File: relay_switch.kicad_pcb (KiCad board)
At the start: 2 copper layers, 37.1 x 73.4 mm, 19 parts, among them P1 POWER, P2 CONN_01X04, P3 INPUT_1, P4 INPUT_2, P5 INPUT_3, P6 INPUT_4, P7 OUTPUT, U1 ULN2003A

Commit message: rerouted pcb
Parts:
- removed REF** (x4): 3.5mmM3, mechanical:3.5mm_m3
- added P10: j_INPUT_2, w_conn_jst-ph:b3b-ph-kl, F.Cu at (208.0, 58.0)
- added P11: j_INPUT_3, w_conn_jst-ph:b3b-ph-kl, F.Cu at (208.0, 76.0)
- added P12: j_INPUT_4, w_conn_jst-ph:b3b-ph-kl, F.Cu at (208.0, 94.0)
- added P13: JST_POWER, w_conn_jst-ph:b2b-ph-kl, F.Cu at (214.5, 22.5)
- added P14: CONN_01X04_jst, w_conn_jst-ph:b4b-ph-kl, F.Cu at (236.0, 40.0)
- added P15: MOUNTING_HOLE, mechanical:3.5mm_m3, F.Cu at (239.5, 20.0)
- added P16: MOUNTING_HOLE, mechanical:3.5mm_m3, F.Cu at (239.5, 106.6)
- added P17: MOUNTING_HOLE, mechanical:3.5mm_m3, F.Cu at (204.0, 20.1)
- added P18: MOUNTING_HOLE, mechanical:3.5mm_m3, F.Cu at (204.0, 106.6)
- added P8: j_OUTPUT, w_conn_screw:mstbva_2,5%2f3-g-5,08, F.Cu at (238.0, 67.0)
- added P9: j_INPUT_1, w_conn_jst-ph:b3b-ph-kl, F.Cu at (208.0, 40.0)
- P3, P4, P5, P6, P7: footprint Pin_Headers:Pin_Header_Straight_1x03 -> w_conn_screw:mstbva_2,5%2f3-g-5,08
- RLY1, RLY2, RLY3, RLY4: footprint Relays_ThroughHole:RY12w-k -> Relays_ThroughHole:RY12w-k_bigger_holes
- moved P7 129.1 mm to (271.0, 71.0), turned to 270 degrees
- moved RLY1 116.0 mm to (231.5, 45.0), turned to 180 degrees
- moved RLY2 114.3 mm to (231.7, 63.1), turned to 180 degrees
- moved RLY3 113.0 mm to (231.7, 80.6), turned to 180 degrees
- moved RLY4 111.3 mm to (231.5, 99.0), turned to 180 degrees
- moved D1 104.3 mm to (225.5, 21.0), turned to 180 degrees
- moved U1 103.5 mm to (221.9, 29.2)
- moved R1 101.8 mm to (235.0, 28.5), turned to 90 degrees
- moved P2 101.7 mm to (233.5, 36.5), turned to 0 degrees
- moved P3 99.3 mm to (205.0, 40.0), turned to 90 degrees
- moved P4 96.8 mm to (205.0, 58.0), turned to 90 degrees
- moved P5 94.5 mm to (205.0, 76.0), turned to 90 degrees
- moved P7 94.1 mm to (234.5, 64.5)
- moved P6 92.5 mm to (205.0, 94.0), turned to 90 degrees
- moved P1 87.2 mm to (215.5, 20.5), turned to 270 degrees
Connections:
- RLY1 pad 8: GND -> +12V
- RLY2 pad 8: GND -> +12V
- RLY3 pad 8: GND -> +12V
- RLY4 pad 8: GND -> +12V
- U1 pad 9: +12V -> GND
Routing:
- net GND: track 128.1 -> 25.3 mm
- net +12V: track 15.5 -> 92.8 mm, vias 1 -> 0
- net R_OUT: track 54.4 -> 88.9 mm, vias 2 -> 0
- net L_OUT: track 57.8 -> 84.9 mm, vias 0 -> 1
- net Net-(P14-Pad4): track 6.83 -> 26.5 mm
- net Net-(P14-Pad3): track 6.83 -> 23.1 mm
- net Net-(P14-Pad2): track 6.83 -> 18.8 mm
- net Net-(RLY4-Pad1): track 56.9 -> 67.9 mm
- net R2_GND: track 97.0 -> 106.4 mm, vias 3 -> 0
- net Net-(P14-Pad1): track 7.40 -> 15.5 mm
- net Net-(RLY3-Pad1): track 42.2 -> 48.6 mm
- net R4_L_IN: track 20.1 -> 14.6 mm
- net R1_L_IN: track 19.0 -> 14.6 mm
- net Net-(D1-Pad1): track 15.5 -> 11.1 mm, vias 1 -> 0
- net Net-(RLY1-Pad1): track 18.5 -> 14.2 mm
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- removed copper zone on B.Cu, net R2_GND
- removed copper zone on F.Cu, net R2_GND
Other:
- board size 37.1 x 73.4 mm -> 229.9 x 105.2 mm

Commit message: couple misc changes, trying to finalize the pcb
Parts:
- moved P7 35.6 mm to (238.4, 85.4)
- moved P14 3.38 mm to (239.3, 40.5)
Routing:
- net Net-(P14-Pad1): track 15.5 -> 20.3 mm
- net Net-(P14-Pad3): track 23.1 -> 27.0 mm
- net Net-(P14-Pad2): track 18.8 -> 22.4 mm
- net Net-(P14-Pad4): track 26.5 -> 29.6 mm
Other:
- board size 229.9 x 105.2 mm -> 41.5 x 92.5 mm
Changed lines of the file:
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@@
-(kicad_pcb (version 4) (host pcbnew 0.201506172246+5766~23~ubuntu14.04.1-product)
+(kicad_pcb (version 4) (host pcbnew 0.201508290901+6132~28~ubuntu14.04.1-product)
   (general
     (links 61)
-    (no_connects 61)
-    (area 115.519999 67.767999 152.704001 141.274001)
+    (no_connects 4)
+    (area 200.949999 16.949999 242.550001 109.550001)
     (thickness 1.6)
-    (drawings 173)
-    (tracks 187)
+    (drawings 171)
+    (tracks 191)
     (zones 0)
     (modules 26)
@@
   )
   (setup
-    (last_trace_width 0.75)
+    (last_trace_width 0.25)
     (user_trace_width 0.75)
     (trace_clearance 0.2)
@@
   )
   (module w_conn_screw:mstbva_2,5%2f3-g-5,08 (layer F.Cu)
-    (at 271 71 270)
+    (at 238.4044 85.3694 270)
     (descr "Terminal block 3 pins, Phoenix MSTBVA 2,5/3-G-5,08")
     (tags DEV)
@@
   )
   (module w_conn_jst-ph:b4b-ph-kl (layer F.Cu)
-    (at 236 40.00228 270)
+    (at 239.3442 40.48506 270)
     (descr "JST PH series connector, B4B-PH-KL")
     (fp_text reference P14 (at 0 -2.99974 270) (layer F.SilkS)
@@
     )
   )
+  (dimension 92.5068 (width 0.3) (layer Eco2.User)
+    (gr_text "92.507 mm" (at 252.556 63.246 270) (layer Eco2.User)
+      (effects (font (size 1.5 1.5) (thickness 0.3)))
+    )
+    (feature1 (pts (xy 242.4938 109.4994) (xy 253.906 109.4994)))
+    (feature2 (pts (xy 242.4938 16.9926) (xy 253.906 16.9926)))
+    (crossbar (pts (xy 251.206 16.9926) (xy 251.206 109.4994)))
+    (arrow1a (pts (xy 251.206 109.4994) (xy 250.619579 108.372896)))
+    (arrow1b (pts (xy 251.206 109.4994) (xy 251.792421 108.372896)))
+    (arrow2a (pts (xy 251.206 16.9926) (xy 250.619579 18.119104)))
+    (arrow2b (pts (xy 251.206 16.9926) (xy 251.792421 18.119104)))
+  )
+  (dimension 41.4782 (width 0.3) (layer Eco2.User)
+    (gr_text "41.478 mm" (at 221.7547 116.666) (layer Eco2.User)
+      (effects (font (size 1.5 1.5) (thickness 0.3)))
+    )
+    (feature1 (pts (xy 242.4938 109.4994) (xy 242.4938 118.016)))
+    (feature2 (pts (xy 201.0156 109.4994) (xy 201.0156 118.016)))
+    (crossbar (pts (xy 201.0156 115.316) (xy 242.4938 115.316)))
+    (arrow1a (pts (xy 242.4938 115.316) (xy 241.367296 115.902421)))
+    (arrow1b (pts (xy 242.4938 115.316) (xy 241.367296 114.729579)))
+    (arrow2a (pts (xy 201.0156 115.316) (xy 202.142104 115.902421)))
+    (arrow2b (pts (xy 201.0156 115.316) (xy 202.142104 114.729579)))
+  )
   (gr_line (start 201 17) (end 242.5 17) (layer Edge.Cuts) (width 0.1))
   (gr_line (start 201 109.5) (end 201 17) (layer Edge.Cuts) (width 0.1))
@@
   (gr_line (start 148.844 80.518) (end 152.4 80.518) (angle 90) (layer B.SilkS) (width 0.2))
   (gr_line (start 148.844 74.422) (end 148.844 80.518) (angle 90) (layer B.SilkS) (width 0.2))
-  (gr_line (start 49.654 122.224) (end 49.654 48.818) (angle 90) (layer Edge.Cuts) (width 0.1))
-  (gr_line (start 12.57 122.224) (end 49.654 122.224) (angle 90) (layer Edge.Cuts) (width 0.1))
-  (gr_line (start 12.57 48.818) (end 12.57 122.224) (angle 90) (layer Edge.Cuts) (width 0.1))
-  (gr_line (start 49.654 48.818) (end 12.57 48.818) (angle 90) (layer Edge.Cuts) (width 0.1))
   (gr_text G (at 148.336 75.438 90) (layer B.SilkS)
     (effects (font (size 0.8 0.8) (thickness 0.1)) (justify mirror))
@@
   (segment (start 208 57.99848) (end 205.00152 57.99848) (width 0.75) (layer F.Cu) (net 18))
   (segment (start 205.00152 57.99848) (end 205 58) (width 0.75) (layer F.Cu) (net 18))
+  (segment (start 233.5 36.46) (end 239.17086 36.46) (width 0.25) (layer F.Cu) (net 19))
+  (segment (start 239.17086 36.46) (end 239.3442 36.63334) (width 0.25) (layer F.Cu) (net 19))
+  (segment (start 239.3442 36.63334) (end 239.3442 37.48278) (width 0.25) (layer F.Cu) (net 19))
   (segment (start 233.5 36.46) (end 233.5 27.1515) (width 0.25) (layer F.Cu) (net 19))
   (segment (start 233.5 27.1515) (end 231.7285 25.38) (width 0.25) (layer F.Cu) (net 19))
   (segment (start 231.7285 25.38) (end 230.78 25.38) (width 0.25) (layer F.Cu) (net 19))
-  (segment (start 236 37) (end 234.04 37) (width 0.25) (layer F.Cu) (net 19))
   (segment (start 234.04 37) (end 233.5 36.46) (width 0.25) (layer F.Cu) (net 19))
+  (segment (start 233.5 39) (end 238.8599 39) (width 0.25) (layer F.Cu) (net 20))
+  (segment (start 238.8599 39) (end 239.3442 39.4843) (width 0.25) (layer F.Cu) (net 20))
   (segment (start 228.24 25.38) (end 228.38 25.38) (width 0.25) (layer F.Cu) (net 20))
   (segment (start 228.38 25.38) (end 231.5 28.5) (width 0.25) (layer F.Cu) (net 20))
@@
   (segment (start 232.5 37.648601) (end 232.5 38.1524) (width 0.25) (layer F.Cu) (net 20))
   (segment (start 233.3476 39) (end 233.5 39) (width 0.25) (layer F.Cu) (net 20))
-  (segment (start 236 39.00152) (end 233.50152 39.00152) (width 0.25) (layer F.Cu) (net 20))
   (segment (start 233.50152 39.00152) (end 233.5 39) (width 0.25) (layer F.Cu) (net 20))
+  (segment (start 233.5 41.54) (end 239.29002 41.54) (width 0.25) (layer F.Cu) (net 21))
+  (segment (start 239.29002 41.54) (end 239.3442 41.48582) (width 0.25) (layer F.Cu) (net 21))
   (segment (start 225.7 25.38) (end 226.38 25.38) (width 0.25) (layer F.Cu) (net 21))
   (segment (start 226.38 25.38) (end 230 29) (width 0.25) (layer F.Cu) (net 21))
@@
   (segment (start 231.5 39.6924) (end 233.3476 41.54) (width 0.25) (layer F.Cu) (net 21))
   (segment (start 233.3476 41.54) (end 233.5 41.54) (width 0.25) (layer F.Cu) (net 21))
-  (segment (start 236 41.00304) (end 234.03696 41.00304) (width 0.25) (layer F.Cu) (net 21))
   (segment (start 234.03696 41.00304) (end 233.5 41.54) (width 0.25) (layer F.Cu) (net 21))
+  (segment (start 233.5 44.08) (end 238.749 44.08) (width 0.25) (layer F.Cu) (net 22))
+  (segment (start 238.749 44.08) (end 239.3442 43.4848) (width 0.25) (layer F.Cu) (net 22))
   (segment (start 223.16 25.38) (end 223.88 25.38) (width 0.25) (layer F.Cu) (net 22))
   (segment (start 229.204999 32.450217) (end 229.263501 32.508719) (width 0.25) (layer F.Cu) (net 22))
@@
   (segment (start 230.5 41.2324) (end 233.3476 44.08) (width 0.25) (layer F.Cu) (net 22))
   (segment (start 233.3476 44.08) (end 233.5 44.08) (width 0.25) (layer F.Cu) (net 22))
-  (segment (start 236 43.00202) (end 234.57798 43.00202) (width 0.25) (layer F.Cu) (net 22))
-  (segment (start 234.57798 43.00202) (end 233.5 44.08) (width 0.25) (layer F.Cu) (net 22))
 )

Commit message: board almost finished
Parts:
- removed P15, P16, P17, P18: MOUNTING_HOLE, mechanical:3.5mm_m3
- removed P5: INPUT_3, w_conn_screw:mstbva_2,5%2f3-g-5,08
- removed P6: INPUT_4, w_conn_screw:mstbva_2,5%2f3-g-5,08
- removed P7: OUTPUT, Pin_Headers:Pin_Header_Straight_1x03
- removed P7: OUTPUT, w_conn_screw:mstbva_2,5%2f3-g-5,08
- D1: footprint LEDs:LED-5MM -> LEDs:LED-1206
- P1: value POWER -> board_mount; footprint Pin_Headers:Pin_Header_Straight_1x02 -> mechanical:3.5mm_m3
- P10: value j_INPUT_2 -> INPUT2
- P11: value j_INPUT_3 -> INPUT3
- P12: value j_INPUT_4 -> INPUT4
- P13: value JST_POWER -> 12vdc
- P14: value CONN_01X04_jst -> J_CONN_01X04
- P2: value CONN_01X04 -> board_mount; footprint Pin_Headers:Pin_Header_Straight_1x04 -> mechanical:3.5mm_m3
- P3: value INPUT_1 -> board_mount; footprint w_conn_screw:mstbva_2,5%2f3-g-5,08 -> mechanical:3.5mm_m3
- P4: value INPUT_2 -> board_mount; footprint w_conn_screw:mstbva_2,5%2f3-g-5,08 -> mechanical:3.5mm_m3
- P8: value j_OUTPUT -> OUTPUT; footprint w_conn_screw:mstbva_2,5%2f3-g-5,08 -> w_conn_jst-ph:b3b-ph-kl
- P9: value j_INPUT_1 -> INPUT1
- R1: footprint Resistors_ThroughHole:Resistor_Horizontal_RM10mm -> Resistors_SMD:R_1206_HandSoldering; moved to B.Cu
- U1: footprint Sockets_DIP:DIP-16__300 -> Housings_SSOP:SSOP-16_4.4x5.2mm_Pitch0.65mm
- moved P2 163.1 mm to (134.5, 166.1)
- moved P1 157.9 mm to (154.2, 166.0), turned to 0 degrees
- moved P8 135.2 mm to (145.5, 165.6), turned to 0 degrees
- moved R1 123.2 mm to (147.7, 115.4), turned to 0 degrees
- moved U1 121.1 mm to (139.6, 118.0), turned to 0 degrees
- moved P14 119.9 mm to (142.9, 111.7), turned to 180 degrees
- moved D1 117.9 mm to (149.6, 111.2), turned to 270 degrees
- moved RLY1 114.0 mm to (156.9, 131.2)
- moved P9 114.0 mm to (133.6, 126.3)
- moved P13 113.0 mm to (153.9, 117.9), turned to 90 degrees
- moved RLY2 108.3 mm to (157.0, 141.5)
- moved P10 108.2 mm to (133.6, 136.6)
- moved RLY3 103.4 mm to (157.0, 152.1)
- moved P11 103.2 mm to (133.7, 147.5)
- moved P3 100.4 mm to (134.5, 111.5), turned to 0 degrees
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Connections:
- P1 pad 1: +12V -> (no net)
- P10 pad 2: R2_GND -> G_OUT
- P11 pad 2: R2_GND -> G_OUT
- P12 pad 2: R2_GND -> G_OUT
- P14 pad 1: Net-(P14-Pad1) -> T1
- P14 pad 2: Net-(P14-Pad2) -> T2
- P14 pad 3: Net-(P14-Pad3) -> T3
- P14 pad 4: Net-(P14-Pad4) -> T4
- P2 pad 1: Net-(P14-Pad1) -> (no net)
- P3 pad 1: R1_R_IN -> (no net)
- P4 pad 1: R2_R_IN -> (no net)
- P8 pad 2: R2_GND -> G_OUT
- P9 pad 2: R2_GND -> G_OUT
- RLY1 pad 2: Net-(RLY1-Pad2) -> (no net)
- RLY1 pad 7: Net-(RLY1-Pad7) -> (no net)
- RLY2 pad 2: Net-(RLY2-Pad2) -> (no net)
- RLY2 pad 7: Net-(RLY2-Pad7) -> (no net)
- RLY3 pad 2: Net-(RLY3-Pad2) -> (no net)
- RLY3 pad 7: Net-(RLY3-Pad7) -> (no net)
- RLY4 pad 2: Net-(RLY4-Pad2) -> (no net)
- RLY4 pad 7: Net-(RLY4-Pad7) -> (no net)
- U1 pad 1: Net-(P14-Pad1) -> T1
- U1 pad 10: Net-(U1-Pad10) -> (no net)
- U1 pad 11: Net-(U1-Pad11) -> (no net)
- U1 pad 12: Net-(U1-Pad12) -> (no net)
- U1 pad 2: Net-(P14-Pad2) -> T2
- U1 pad 3: Net-(P14-Pad3) -> T3
- U1 pad 4: Net-(P14-Pad4) -> T4
- U1 pad 5: Net-(U1-Pad5) -> (no net)
- U1 pad 6: Net-(U1-Pad6) -> (no net)
- U1 pad 7: Net-(U1-Pad7) -> (no net)
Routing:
- net R2_GND: track 106.4 -> 0.00 mm
- net G_OUT: track 0.00 -> 59.0 mm
- net R_OUT: track 88.9 -> 41.8 mm
- net +12V: track 92.8 -> 48.7 mm, vias 0 -> 1
- net L_OUT: track 84.9 -> 52.9 mm, vias 1 -> 0
- net Net-(P14-Pad4): track 29.6 -> 0.00 mm
- net Net-(P14-Pad3): track 27.0 -> 0.00 mm
- net Net-(P14-Pad2): track 22.4 -> 0.00 mm
- net Net-(P14-Pad1): track 20.3 -> 0.00 mm
- net Net-(RLY4-Pad1): track 67.9 -> 51.1 mm
- net T1: track 0.00 -> 11.0 mm, vias 0 -> 1
- net T2: track 0.00 -> 10.1 mm
- net T3: track 0.00 -> 10.0 mm, vias 0 -> 1
- net T4: track 0.00 -> 8.78 mm, vias 0 -> 1
- net Net-(RLY1-Pad1): track 14.2 -> 22.3 mm
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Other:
- board size 41.5 x 92.5 mm -> 25.6 x 60.4 mm
- board text added: "12vdc"
- board text added: "2016"
- board text added: "INPUT1"
- board text added: "INPUT3"
- board text added: "INPUT4"
- board text added: "L.IN"
- board text added: "L.OUT"
- board text added: "R.IN"
- board text added: "R.OUT"
- board text added: "jjrh"
- board text removed: "10"
- board text removed: "10k"
- board text removed: "11"
- board text removed: "12"
- board text removed: "13"
- board text removed: "14"
- board text removed: "15"
- board text removed: "5"
- board text removed: "6"
- board text removed: "7"
- board text removed: "GND"
- board text removed: "INPUT 1"
- board text removed: "INPUT 2"
- board text removed: "INPUT 3"
- board text removed: "INPUT 4"
- board text removed: "INPUT BOARD V1"
- board text removed: "L"
- board text removed: "R"
- board text removed: "ULN2003A"
- board text removed: "jjrh 2015"

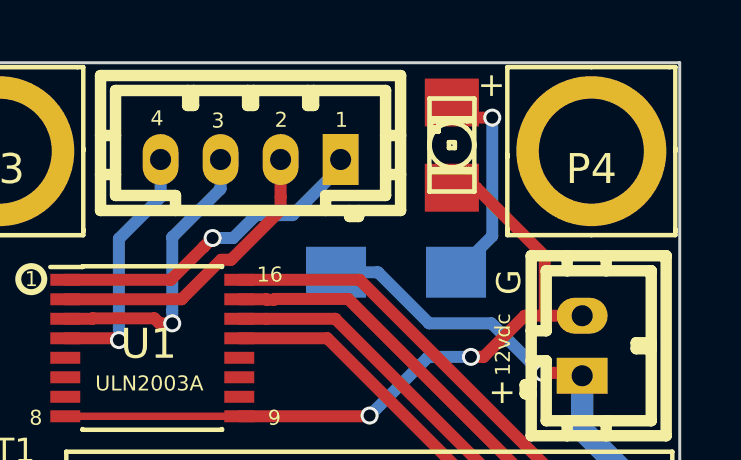
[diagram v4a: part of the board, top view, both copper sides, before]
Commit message: set 3d footprint for the led
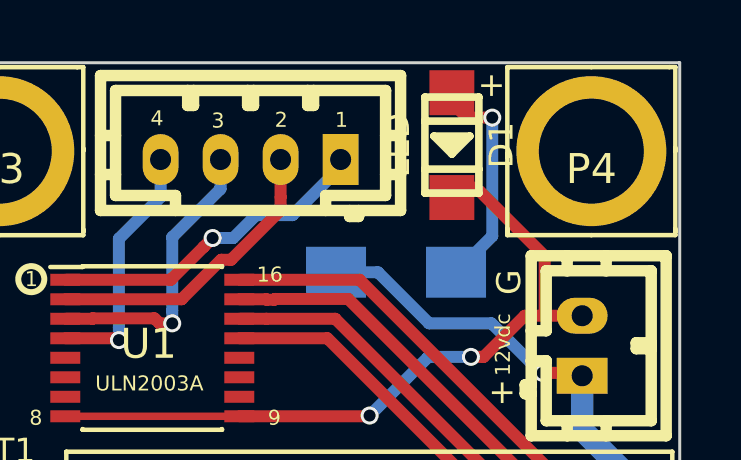
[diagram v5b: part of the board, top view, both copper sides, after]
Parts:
- D1: footprint LEDs:LED-1206 -> w_smd_leds:Led_1206
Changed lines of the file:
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@@
     )
-  )
-  (module LEDs:LED-1206 (layer F.Cu)
-    (at 149.5806 111.20374 270)
-    (descr "LED 1206 smd package")
-    (tags "LED1206 SMD")
-    (attr smd)
-    (fp_text reference D1 (at 0.254 -1.524 270) (layer F.SilkS) hide
-      (effects (font (size 1 1) (thickness 0.15)))
-    )
-    (fp_text value LED (at 0 1.65 270) (layer F.Fab) hide
-      (effects (font (size 1 1) (thickness 0.15)))
-    )
-    (fp_line (start 0.09906 0.09906) (end -0.09906 0.09906) (layer F.SilkS) (width 0.15))
-    (fp_line (start -0.09906 0.09906) (end -0.09906 -0.09906) (layer F.SilkS) (width 0.15))
-    (fp_line (start 0.09906 -0.09906) (end -0.09906 -0.09906) (layer F.SilkS) (width 0.15))
-    (fp_line (start 0.09906 0.09906) (end 0.09906 -0.09906) (layer F.SilkS) (width 0.15))
-    (fp_line (start -0.44958 0.6985) (end -0.79756 0.6985) (layer F.SilkS) (width 0.15))
-    (fp_line (start -0.79756 0.6985) (end -0.79756 0.44958) (layer F.SilkS) (width 0.15))
-    (fp_line (start -0.44958 0.44958) (end -0.79756 0.44958) (layer F.SilkS) (width 0.15))
-    (fp_line (start -0.44958 0.6985) (end -0.44958 0.44958) (layer F.SilkS) (width 0.15))
-    (fp_line (start -0.79756 0.6985) (end -0.89916 0.6985) (layer F.SilkS) (width 0.15))
-    (fp_line (start -0.89916 0.6985) (end -0.89916 -0.49784) (layer F.SilkS) (width 0.15))
-    (fp_line (start -0.79756 -0.49784) (end -0.89916 -0.49784) (layer F.SilkS) (width 0.15))
-    (fp_line (start -0.79756 0.6985) (end -0.79756 -0.49784) (layer F.SilkS) (width 0.15))
-    (fp_line (start -0.79756 -0.54864) (end -0.89916 -0.54864) (layer F.SilkS) (width 0.15))
-    (fp_line (start -0.89916 -0.54864) (end -0.89916 -0.6985) (layer F.SilkS) (width 0.15))
-    (fp_line (start -0.79756 -0.6985) (end -0.89916 -0.6985) (layer F.SilkS) (width 0.15))
-    (fp_line (start -0.79756 -0.54864) (end -0.79756 -0.6985) (layer F.SilkS) (width 0.15))
-    (fp_line (start 0.89916 0.6985) (end 0.79756 0.6985) (layer F.SilkS) (width 0.15))
-    (fp_line (start 0.79756 0.6985) (end 0.79756 -0.49784) (layer F.SilkS) (width 0.15))
-    (fp_line (start 0.89916 -0.49784) (end 0.79756 -0.49784) (layer F.SilkS) (width 0.15))
-    (fp_line (start 0.89916 0.6985) (end 0.89916 -0.49784) (layer F.SilkS) (width 0.15))
-    (fp_line (start 0.89916 -0.54864) (end 0.79756 -0.54864) (layer F.SilkS) (width 0.15))
-    (fp_line (start 0.79756 -0.54864) (end 0.79756 -0.6985) (layer F.SilkS) (width 0.15))
-    (fp_line (start 0.89916 -0.6985) (end 0.79756 -0.6985) (layer F.SilkS) (width 0.15))
-    (fp_line (start 0.89916 -0.54864) (end 0.89916 -0.6985) (layer F.SilkS) (width 0.15))
-    (fp_line (start -0.44958 0.6985) (end -0.59944 0.6985) (layer F.SilkS) (width 0.15))
-    (fp_line (start -0.59944 0.6985) (end -0.59944 0.44958) (layer F.SilkS) (width 0.15))
-    (fp_line (start -0.44958 0.44958) (end -0.59944 0.44958) (layer F.SilkS) (width 0.15))
-    (fp_line (start -0.44958 0.6985) (end -0.44958 0.44958) (layer F.SilkS) (width 0.15))
-    (fp_line (start -1.5494 0.7493) (end 1.5494 0.7493) (layer F.SilkS) (width 0.15))
-    (fp_line (start 1.5494 0.7493) (end 1.5494 -0.7493) (layer F.SilkS) (width 0.15))
-    (fp_line (start 1.5494 -0.7493) (end -1.5494 -0.7493) (layer F.SilkS) (width 0.15))
-    (fp_line (start -1.5494 -0.7493) (end -1.5494 0.7493) (layer F.SilkS) (width 0.15))
-    (fp_arc (start 0 0) (end -0.54864 0.49784) (angle -95.4) (layer F.SilkS) (width 0.15))
-    (fp_arc (start 0 0) (end 0.54864 0.49784) (angle -84.5) (layer F.SilkS) (width 0.15))
-    (fp_arc (start 0 0) (end 0.54864 -0.49784) (angle -95.4) (layer F.SilkS) (width 0.15))
-    (fp_arc (start 0 0) (end -0.54864 -0.49784) (angle -84.5) (layer F.SilkS) (width 0.15))
-    (pad 2 smd rect (at 1.41986 0 90) (size 1.59766 1.80086) (layers F.Cu F.Paste F.Mask)
-      (net 1 GND))
-    (pad 1 smd rect (at -1.41986 0 90) (size 1.59766 1.80086) (layers F.Cu F.Paste F.Mask)
-      (net 2 "Net-(D1-Pad1)"))
   )
   (module mechanical:3.5mm_m3 (layer F.Cu)
@@
       (at (xyz 0 0 0))
       (scale (xyz 1 1 1))
+      (rotate (xyz 0 0 0))
+    )
+  )
+  (module w_smd_leds:Led_1206 (layer F.Cu)
+    (at 149.5806 111.20374 270)
+    (descr "SMD LED, 1206")
+    (fp_text reference D1 (at 0 -1.651 270) (layer F.SilkS)
+      (effects (font (size 0.8001 0.8001) (thickness 0.14986)))
+    )
+    (fp_text value LED (at 0 1.80086 270) (layer F.SilkS)
+      (effects (font (size 0.8001 0.8001) (thickness 0.14986)))
+    )
+    (fp_line (start 0 -0.20066) (end 0 0.09906) (layer F.SilkS) (width 0.254))
+    (fp_line (start -0.09906 0.29972) (end -0.09906 -0.29972) (layer F.SilkS) (width 0.254))
+    (fp_line (start -0.29972 -0.59944) (end -0.29972 0.59944) (layer F.SilkS) (width 0.254))
+    (fp_line (start -0.29972 0.59944) (end 0.29972 0) (layer F.SilkS) (width 0.254))
+    (fp_line (start 0.29972 0) (end -0.29972 -0.59944) (layer F.SilkS) (width 0.254))
+    (fp_line (start 0.8001 0.89916) (end 0.8001 -0.89916) (layer F.SilkS) (width 0.254))
+    (fp_line (start -0.8001 -0.89916) (end -0.8001 0.89916) (layer F.SilkS) (width 0.254))
+    (fp_line (start -1.6002 -0.89916) (end 1.6002 -0.89916) (layer F.SilkS) (width 0.254))
+    (fp_line (start 1.6002 -0.89916) (end 1.6002 0.89916) (layer F.SilkS) (width 0.254))
+    (fp_line (start 1.6002 0.89916) (end -1.6002 0.89916) (layer F.SilkS) (width 0.254))
+    (fp_line (start -1.6002 0.89916) (end -1.6002 -0.89916) (layer F.SilkS) (width 0.254))
+    (pad 1 smd rect (at -1.74752 0 270) (size 1.4986 1.4986) (layers F.Cu F.Paste F.Mask)
+      (net 2 "Net-(D1-Pad1)"))
+    (pad 2 smd rect (at 1.74752 0 270) (size 1.4986 1.4986) (layers F.Cu F.Paste F.Mask)
+      (net 1 GND))
+    (model walter/smd_leds/led_1206.wrl
+      (at (xyz 0 0 0))
+      (scale (xyz 1 1 1))

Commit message: board changes and corrections
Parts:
- added C1: 100nF, w_smd_cap:c_1206, B.Cu at (136.2, 117.3)
- added C2: 1000uF, w_capacitors:CP_10x20mm, F.Cu at (146.1, 115.4)
- P13: value 12vdc -> POWER
- P9: value INPUT1 -> INPUT.1
- moved P14 5.44 mm to (142.8, 106.2), turned to 0 degrees
- moved D1 5.06 mm to (154.2, 113.2), turned to 180 degrees
- moved U1 4.81 mm to (136.2, 114.5)
- moved P3 4.22 mm to (134.5, 107.3)
- moved P4 4.22 mm to (154.2, 107.3)
- moved R1 2.38 mm to (150.1, 115.2), turned to 90 degrees
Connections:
- net G_OUT renamed R1_GND
- D1 pad 1: Net-(D1-Pad1) -> GND
- D1 pad 2: GND -> Net-(D1-Pad2)
- R1 pad 2: Net-(D1-Pad1) -> Net-(D1-Pad2)
- U1 pad 9: GND -> +12V
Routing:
- net +12V: track 48.7 -> 58.4 mm
- net Net-(D1-Pad1): track 7.34 -> 0.00 mm, vias 1 -> 0
- net T4: track 8.78 -> 15.9 mm, vias 1 -> 0
- net Net-(RLY1-Pad1): track 22.3 -> 29.2 mm
- net Net-(RLY2-Pad1): track 31.7 -> 38.5 mm
- net Net-(RLY3-Pad1): track 41.4 -> 48.1 mm
- net Net-(RLY4-Pad1): track 51.1 -> 57.7 mm
- net GND: track 24.6 -> 29.1 mm, vias 2 -> 1
- net T3: track 10.0 -> 13.5 mm, vias 1 -> 0
- net Net-(D1-Pad2): track 0.00 -> 2.40 mm, vias 0 -> 1
- net T1: track 11.0 -> 9.13 mm, vias 1 -> 0
- net T2: track 10.1 -> 11.3 mm
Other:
- board size 25.6 x 60.4 mm -> 25.7 x 64.6 mm
